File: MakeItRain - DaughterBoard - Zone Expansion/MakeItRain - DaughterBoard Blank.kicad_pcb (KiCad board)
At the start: 2 copper layers, 121.3 x 68.1 mm, 33 parts, among them J1 Conn_02x14_Odd_Even, P1 Screw_Terminal_01x02, P2 Screw_Terminal_01x02, P3 Screw_Terminal_01x02, P4 Screw_Terminal_01x02, Q1 2N7000, Q2 IRF9Z34NPBF, Q3 2N7000, Q4 IRF9Z34NPBF, Q5 2N7000, Q6 IRF9Z34NPBF, Q7 2N7000, Q8 IRF9Z34NPBF

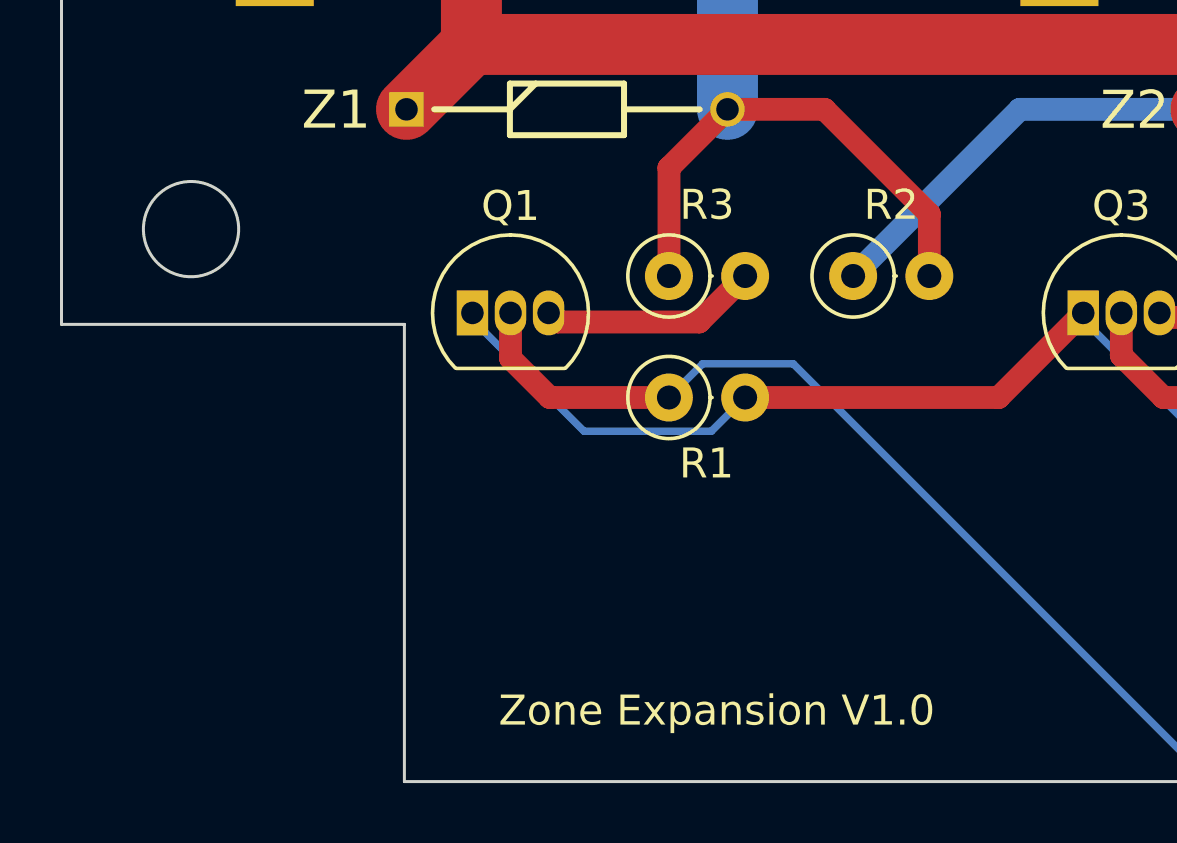
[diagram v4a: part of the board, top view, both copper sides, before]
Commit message: updating the position of one daughter board mounting holes.
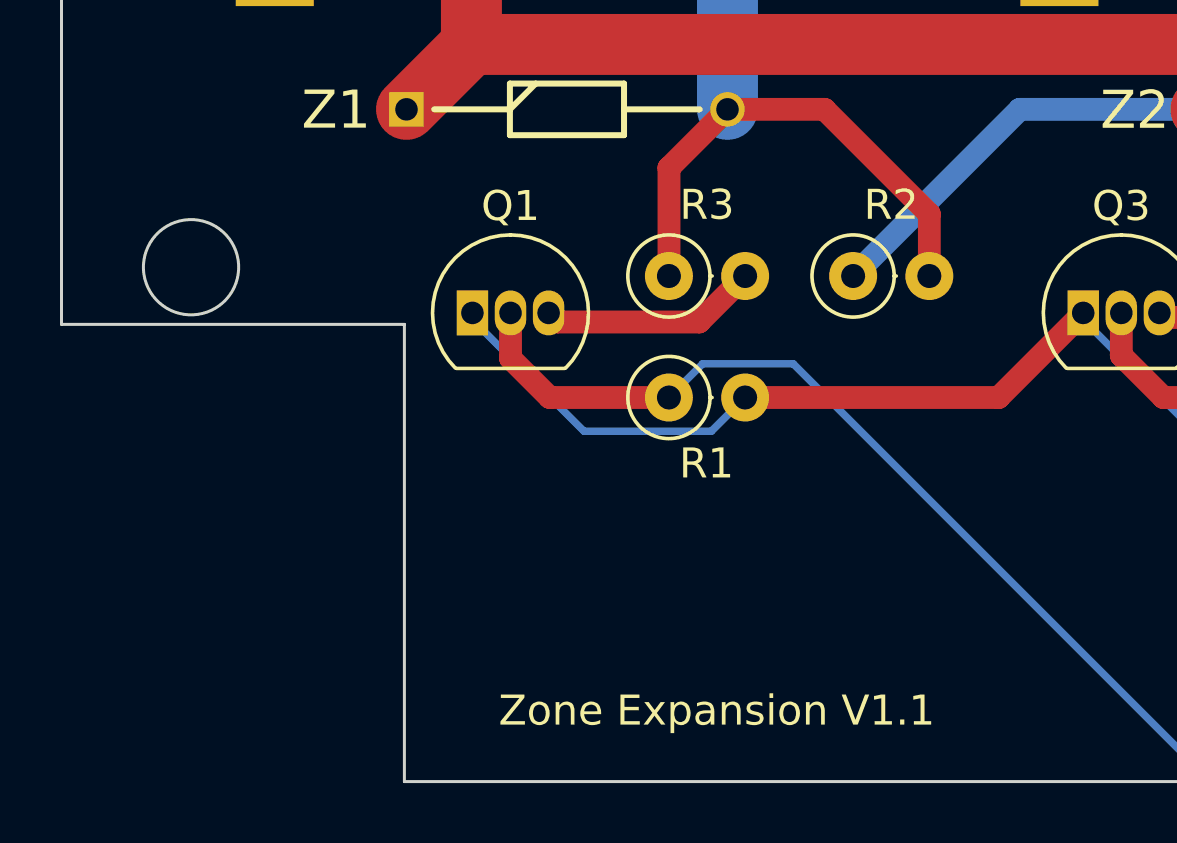
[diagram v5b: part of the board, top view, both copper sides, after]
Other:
- outline, holes or cut-outs redrawn
- board text added: "Zone Expansion V1.1"
- board text removed: "Zone Expansion V1.0"
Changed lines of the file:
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@@
   (gr_line (start 52.07 111.76) (end 52.07 77.47)
     (stroke (width 0.1) (type solid)) (layer "Edge.Cuts"))
-  (gr_circle (center 56.388 108.585) (end 57.9755 108.585)
+  (gr_circle (center 56.388 109.855) (end 57.9755 109.855)
     (stroke (width 0.1) (type solid)) (fill none) (layer "Edge.Cuts"))
   (gr_circle (center 147.418926 108.536569) (end 149.006426 108.536569)
@@
     (effects (font (size 1 1) (thickness 0.15)))
   )
-  (gr_text "Zone Expansion V1.0" (at 73.912049 124.637182) (layer "F.SilkS")
+  (gr_text "Zone Expansion V1.1" (at 73.912049 124.637182) (layer "F.SilkS")
     (effects (font (size 1 1) (thickness 0.15)))
   )
